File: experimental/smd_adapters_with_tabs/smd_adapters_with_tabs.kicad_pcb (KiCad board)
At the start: 2 copper layers, 79.8 x 64.6 mm, 40 parts

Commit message: Flushing pending changes.
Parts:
- removed mouse-bite-2.54mm-slot (x14): VAL**, greenpack_smd_adapters:mouse-bite-2.54mm-slot-external
- removed mouse-bite-2.54mm-slot (x16): VAL**, greenpack_smd_adapters:mouse-bite-2.54mm-slot
- removed mouse-bite-2.54mm-slot (x2): VAL**, greenpack_smd_adapters:mouse-bite-2.54mm-slot-external-short
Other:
- outline, holes or cut-outs redrawn

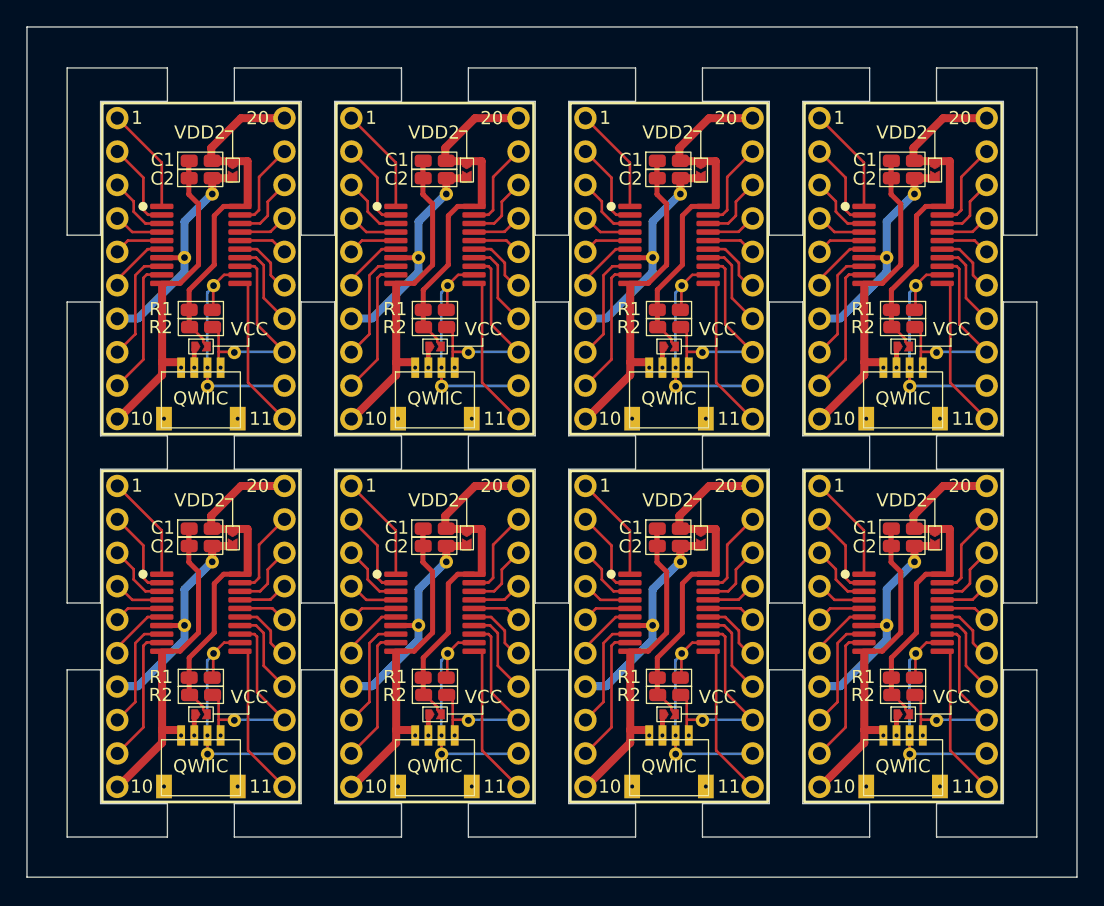
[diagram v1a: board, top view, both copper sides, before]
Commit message: Added SMD adapter schematic. Cleaned up layout and panel.
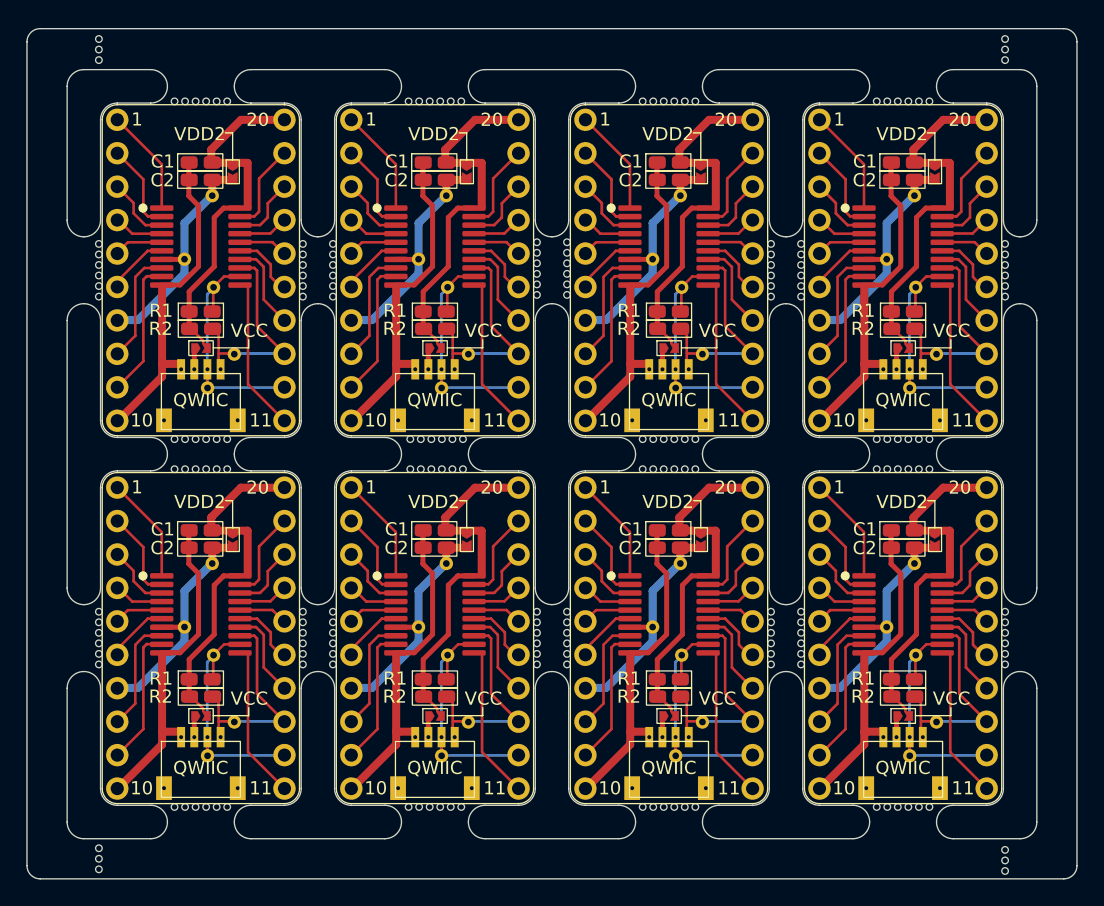
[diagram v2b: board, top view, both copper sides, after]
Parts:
- added mouse-bite-2.54mm-slot: VAL**, greenpack_smd_adapters:mouse-bite-holes-short, F.Cu at (192.0, 127.6)
- added mouse-bite-2.54mm-slot: VAL**, greenpack_smd_adapters:mouse-bite-holes, F.Cu at (183.1, 96.8)
- added mouse-bite-2.54mm-slot: VAL**, greenpack_smd_adapters:mouse-bite-holes, F.Cu at (138.7, 82.8)
- added mouse-bite-2.54mm-slot: VAL**, greenpack_smd_adapters:mouse-bite-holes-short, F.Cu at (192.0, 66.0)
- added mouse-bite-2.54mm-slot: VAL**, greenpack_smd_adapters:mouse-bite-holes-half, F.Cu at (147.6, 124.7)
- added mouse-bite-2.54mm-slot: VAL**, greenpack_smd_adapters:mouse-bite-holes-short, F.Cu at (120.9, 127.5)
- added mouse-bite-2.54mm-slot: VAL**, greenpack_smd_adapters:mouse-bite-holes-half, F.Cu at (120.9, 110.7)
- added mouse-bite-2.54mm-slot: VAL**, greenpack_smd_adapters:mouse-bite-holes, F.Cu at (147.7, 96.8)
- added mouse-bite-2.54mm-slot: VAL**, greenpack_smd_adapters:mouse-bite-holes, F.Cu at (174.2, 110.7)
- added mouse-bite-2.54mm-slot: VAL**, greenpack_smd_adapters:mouse-bite-holes-half, F.Cu at (129.8, 68.8)
- added mouse-bite-2.54mm-slot: VAL**, greenpack_smd_adapters:mouse-bite-holes, F.Cu at (138.7, 110.7)
- added mouse-bite-2.54mm-slot: VAL**, greenpack_smd_adapters:mouse-bite-holes-half, F.Cu at (192.0, 110.7)
- added mouse-bite-2.54mm-slot: VAL**, greenpack_smd_adapters:mouse-bite-holes-half, F.Cu at (147.6, 68.8)
- added mouse-bite-2.54mm-slot: VAL**, greenpack_smd_adapters:mouse-bite-holes, F.Cu at (165.4, 96.8)
- added mouse-bite-2.54mm-slot: VAL**, greenpack_smd_adapters:mouse-bite-holes-short, F.Cu at (120.9, 66.0)
- added mouse-bite-2.54mm-slot: VAL**, greenpack_smd_adapters:mouse-bite-holes-half, F.Cu at (129.8, 124.7)
- added mouse-bite-2.54mm-slot: VAL**, greenpack_smd_adapters:mouse-bite-holes-half, F.Cu at (120.9, 82.8)
- added mouse-bite-2.54mm-slot: VAL**, greenpack_smd_adapters:mouse-bite-holes-half, F.Cu at (183.1, 68.8)
- added mouse-bite-2.54mm-slot: VAL**, greenpack_smd_adapters:mouse-bite-holes, F.Cu at (156.5, 82.7)
- added mouse-bite-2.54mm-slot: VAL**, greenpack_smd_adapters:mouse-bite-holes-half, F.Cu at (183.1, 124.7)
- added mouse-bite-2.54mm-slot: VAL**, greenpack_smd_adapters:mouse-bite-holes-half, F.Cu at (165.4, 68.8)
- added mouse-bite-2.54mm-slot: VAL**, greenpack_smd_adapters:mouse-bite-holes, F.Cu at (156.5, 110.7)
- added mouse-bite-2.54mm-slot: VAL**, greenpack_smd_adapters:mouse-bite-holes-half, F.Cu at (165.4, 124.7)
- added mouse-bite-2.54mm-slot: VAL**, greenpack_smd_adapters:mouse-bite-holes, F.Cu at (174.2, 82.8)
- added mouse-bite-2.54mm-slot: VAL**, greenpack_smd_adapters:mouse-bite-holes-half, F.Cu at (192.0, 82.8)
- added mouse-bite-2.54mm-slot: VAL**, greenpack_smd_adapters:mouse-bite-holes, F.Cu at (129.8, 96.8)
- moved REF** 0.13 mm to (183.1, 110.7)
- moved REF** 0.13 mm to (147.6, 82.8)
- moved REF** 0.13 mm to (147.6, 110.7)
- moved REF** 0.13 mm to (183.1, 82.8)
- moved REF** 0.13 mm to (165.4, 82.8)
- moved REF** 0.13 mm to (129.8, 82.8)
- moved REF** 0.13 mm to (129.8, 110.7)
- moved REF** 0.13 mm to (165.4, 110.7)
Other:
- outline, holes or cut-outs redrawn
